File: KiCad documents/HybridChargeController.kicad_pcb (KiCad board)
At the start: 2 copper layers, 87 x 87 mm, 102 parts, among them P1 Load, P2 LI_balancer, P3 PV, P4 Extra, P5 LI, P6 LA, Q1 MMBT3904, Q10 MMBT3904, Q11 IPD90P04P4L-04, Q12 STL60P4LLF6, Q13 STL60P4LLF6, Q14 IPD90P04P4L-04, Q15 BSS138, Q16 BSS138, Q2 IPD90P04P4L-04, Q3 MMBT3904, Q4 IPD90P04P4L-04, Q5 IPD90P04P4L-04, Q6 MMBT3904, Q7 MMBT3904, Q8 MMBT3904, Q9 IPD90P04P4L-04, U1 LM358D, U2 bq76920, U3 cd4051, U4 LM358D, U5 LM358D

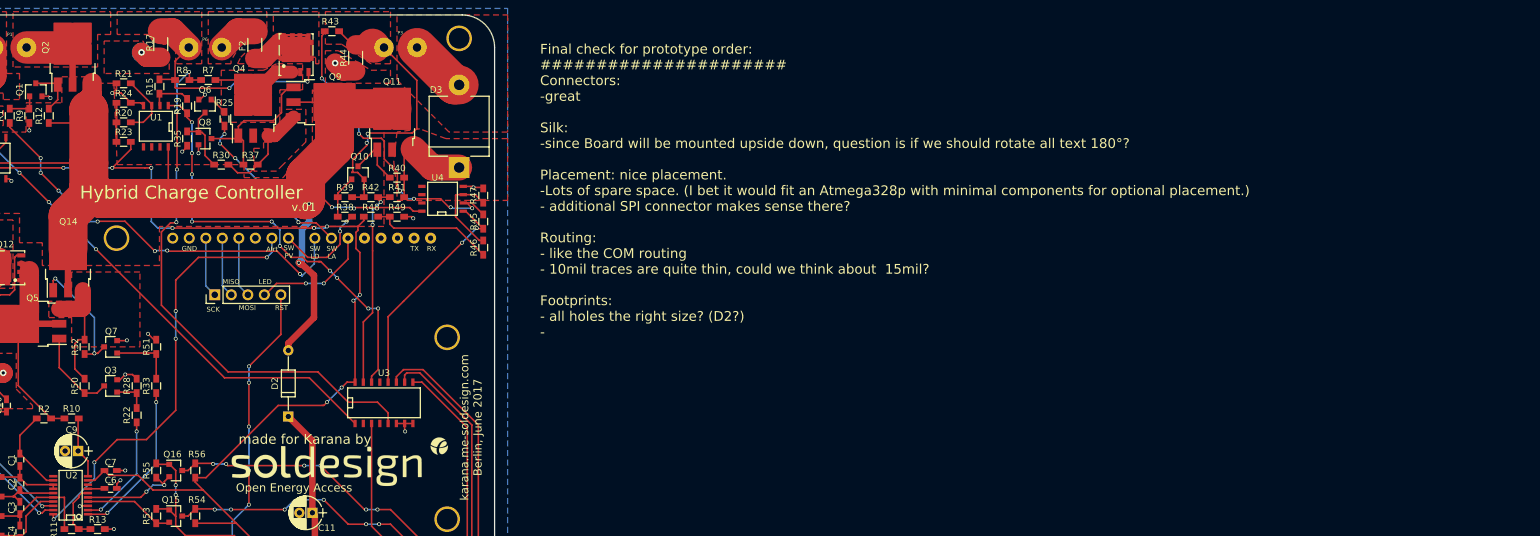
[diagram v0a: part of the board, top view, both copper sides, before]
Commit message: added FTDI connector
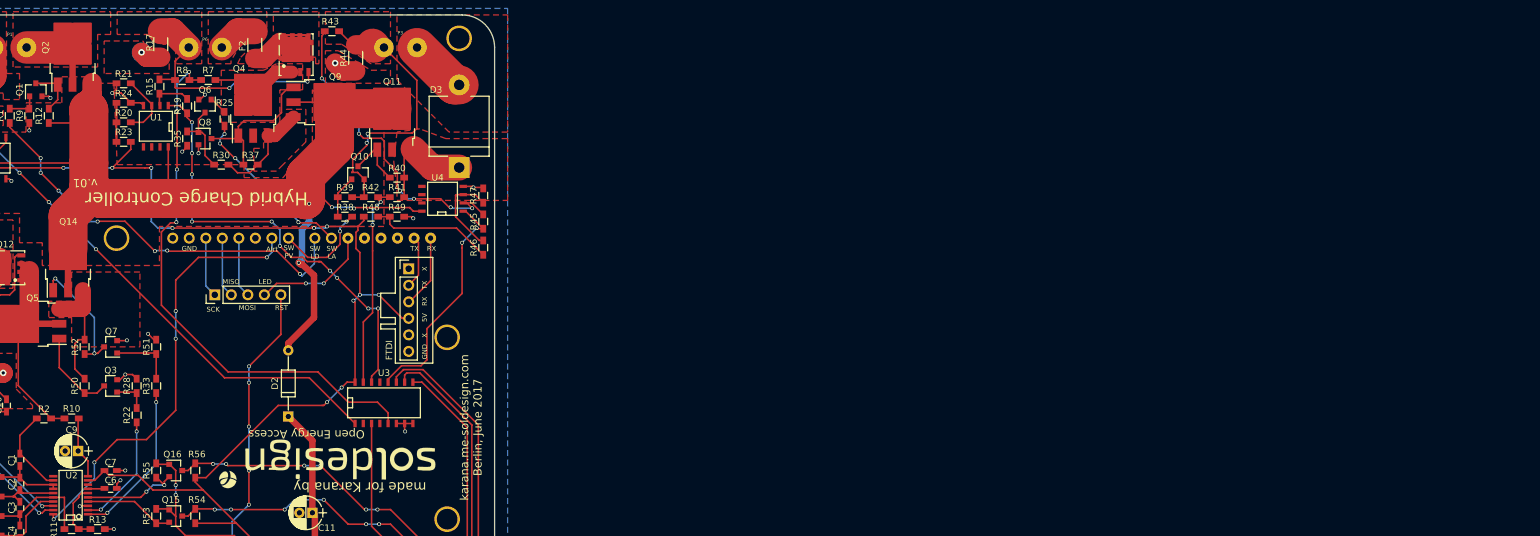
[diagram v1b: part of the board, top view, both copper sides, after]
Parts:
- added FTDI: FTDI, Pin_Headers:Pin_Header_Straight_1x06_Pitch2.54mm, F.Cu at (173.8, 79.0)
- moved G*** 2.33 mm to (161.1, 109.0), turned to 180 degrees
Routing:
- net /RX: track 0.00 -> 11.2 mm
- net /5V: track 175.4 -> 184.4 mm, vias 10 -> 11
- net /TX: track 0.00 -> 8.15 mm
- net /S_PV_I: track 34.5 -> 36.3 mm
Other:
- board text added: "Final check for prototype order: ###################### Placement: nice placement. -Lots of spare space. (I bet it would fit an Atmega328p with minimal components for optional placement.) - additional SPI connector makes sense there? Routing: - like the COM routing - 10mil traces are quite thin, could we think about 15mil? Footprints: - all holes the right size? (D2?) -"
- board text added: "X"
- board text removed: "Final check for prototype order: ###################### Connectors: -great Silk: -since Board will be mounted upside down, question is if we should rotate all text 180°? Placement: nice placement. -Lots of spare space. (I bet it would fit an Atmega328p with minimal components for optional placement.) - additional SPI connector makes sense there? Routing: - like the COM routing - 10mil traces are 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"

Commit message: gerbered like this
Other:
- board text removed: "Final check for prototype order: ###################### Placement: nice placement. -Lots of spare space. (I bet it would fit an Atmega328p with minimal components for optional placement.) - additional SPI connector makes sense there? Routing: - like the COM routing - 10mil traces are quite thin, could we think about 15mil? Footprints: - all holes the right size? (D2?) -"
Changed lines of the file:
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@@
     (links 252)
     (no_connects 2)
-    (area 99.924999 39.924999 187.075001 127.075001)
+    (area 97 39 189.000001 129.000001)
     (thickness 1.6)
-    (drawings 59)
+    (drawings 58)
     (tracks 882)
     (zones 0)
@@
     (visible_elements 7FFEFFFF)
     (pcbplotparams
-      (layerselection 0x00030_80000001)
+      (layerselection 0x010ac_80000001)
       (usegerberextensions false)
       (excludeedgelayer true)
@@
       (psa4output false)
       (plotreference true)
-      (plotvalue true)
+      (plotvalue false)
       (plotinvisibletext false)
       (padsonsilk false)
@@
       (outputformat 1)
       (mirror false)
-      (drillshape 1)
+      (drillshape 0)
       (scaleselection 1)
-      (outputdirectory ""))
+      (outputdirectory Gerbers/))
   )
   (net 0 "")
@@
     (descr "Through hole straight pin header, 1x05, 2.54mm pitch, single row")
     (tags "Through hole pin header THT 1x05 2.54mm single row")
-    (fp_text reference P4 (at 2.5 4.75 180) (layer F.Fab)
+    (fp_text reference P4 (at 2.5 4.75 180) (layer F.Fab) hide
       (effects (font (size 1 1) (thickness 0.15)))
     )
@@
   (gr_line (start 171.75 88.25) (end 169.5 88.25) (angle 90) (layer F.SilkS) (width 0.2))
   (gr_line (start 171.75 93.5) (end 171.75 88.25) (angle 90) (layer F.SilkS) (width 0.2))
-  (gr_text "Final check for prototype order:\n######################\nPlacement: nice placement. \n-Lots of spare space. (I bet it would fit an Atmega328p with minimal components for optional placement.)\n- additional SPI connector makes sense there?\n\nRouting:\n- like the COM routing\n- 10mil traces are quite thin, could we think about  15mil?\n\nFootprints:\n- all holes the right size? (D2?)\n- \n\n" (at 193.9798 68.199) (layer Eco2.User)
-    (effects (font (size 1.5 1.5) (thickness 0.3)) (justify left))
-  )
   (gr_text "karana.me-soldesign.com\nBerlin, June 2017" (at 183.388 103.378 90) (layer F.SilkS)
     (effects (font (size 1.27 1.27) (thickness 0.2032)))
